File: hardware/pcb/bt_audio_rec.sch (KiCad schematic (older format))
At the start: 61 parts, among them IC1 RN52-I_RM116, IC2 VCNL4200, J1 OutL, J13 Power, J14 PROX Socket, J15 PROX Header, J2 AYF333135, J3 RN52 factory reset, J4 ERM, J5 OutR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

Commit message: Change LED resistor
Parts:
- R13: value 3.6R -> 1.8R
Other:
- note added: "1.8R with 3.3V\nsupply = about\n550mA peak current."
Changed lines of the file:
@@
 P 10100 8500
 F 0 "R13" H 10170 8546 50  0000 L CNN
-F 1 "3.6R" H 10170 8455 50  0000 L CNN
+F 1 "1.8R" H 10170 8455 50  0000 L CNN
 F 2 "Resistor_SMD:R_0603_1608Metric" V 10030 8500 50  0001 C CNN
 F 3 "~" H 10100 8500 50  0001 C CNN
@@
 	0    -1   -1   0
 $EndComp
+Text Notes 10400 8650 0    50   ~ 0
+1.8R with 3.3V\nsupply = about\n550mA peak current.
 $EndSCHEMATC

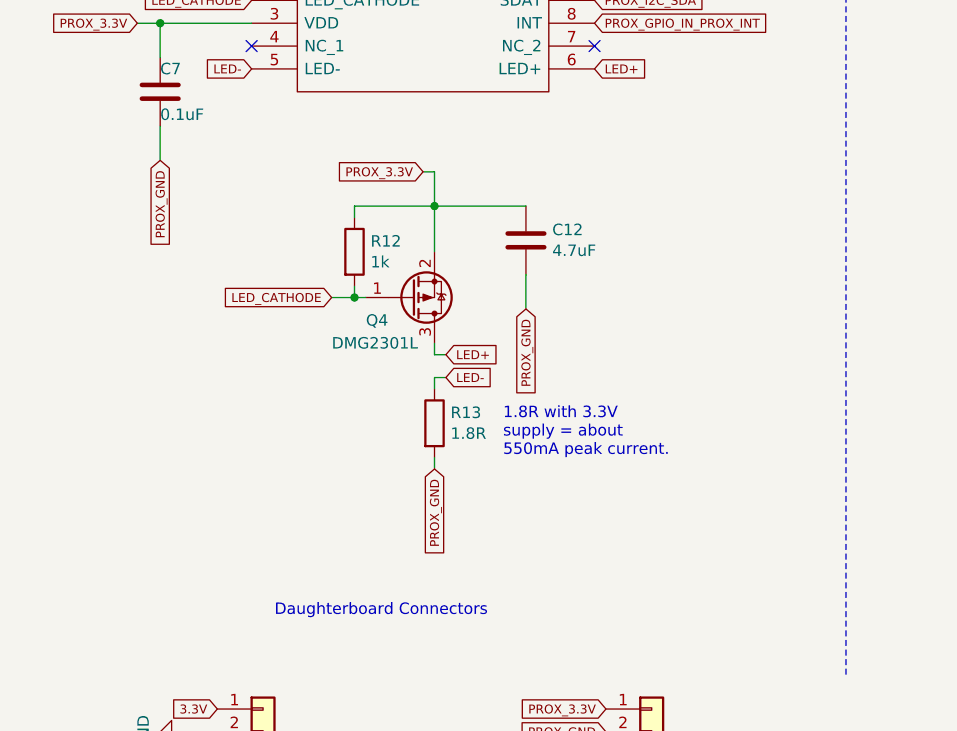
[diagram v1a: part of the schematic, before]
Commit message: Add decoupling cap to proximity LED
See https://www.duk.io/blog/electronics-projects/bt-player/bluetooth-audio-player-firmware
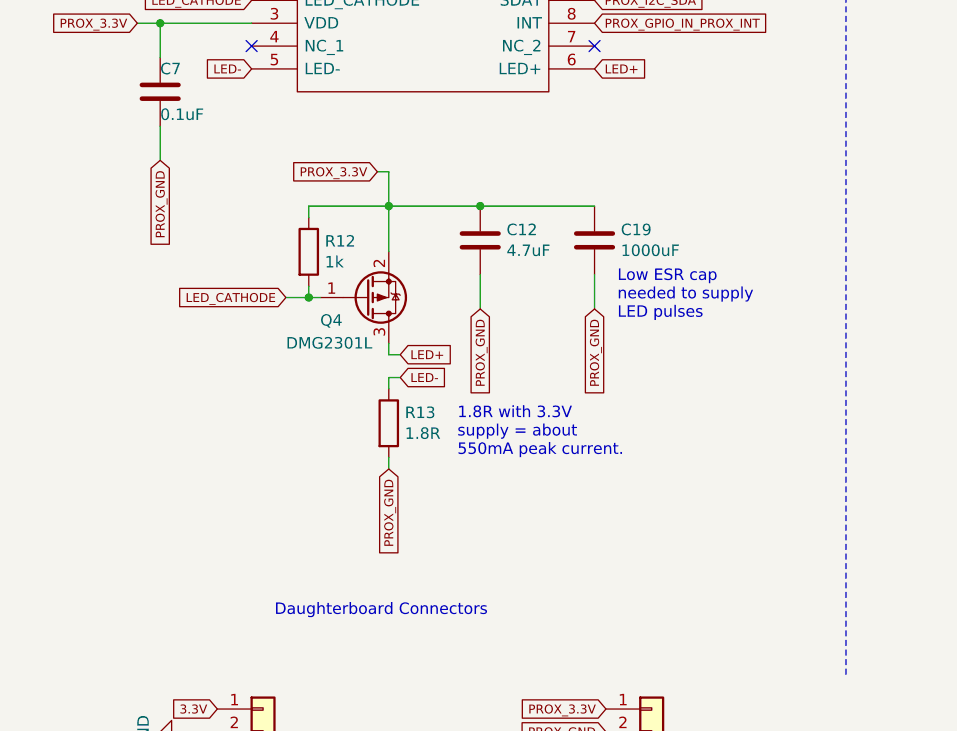
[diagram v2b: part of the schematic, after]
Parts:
- added C19: 1000uF, Capacitor_THT:C_Radial_D6.3mm_H7.0mm_P2.50mm, symbol Device:C
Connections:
- net PROX_3.3V: now also C19.1
- net PROX_GND: now also C19.2
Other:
- note added: "Low ESR cap\nneeded to supply\nLED pulses"
- moved on the sheet: C12, Q4, R12, R13
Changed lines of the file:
@@
 L Transistor_FET:DMG2301L Q4
 U 1 1 5ED5A120
-P 10000 7950
-F 0 "Q4" H 9800 8050 50  0000 L CNN
-F 1 "DMG2301L" H 9650 8150 50  0000 L CNN
-F 2 "Package_TO_SOT_SMD:SOT-23" H 10200 7875 50  0001 L CIN
-F 3 "https://www.diodes.com/assets/Datasheets/DMG2301L.pdf" H 10000 7950 50  0001 L CNN
-	1    10000 7950
+P 9800 7950
+F 0 "Q4" H 9600 8050 50  0000 L CNN
+F 1 "DMG2301L" H 9450 8150 50  0000 L CNN
+F 2 "Package_TO_SOT_SMD:SOT-23" H 10000 7875 50  0001 L CIN
+F 3 "https://www.diodes.com/assets/Datasheets/DMG2301L.pdf" H 9800 7950 50  0001 L CNN
+	1    9800 7950
 	1    0    0    1
 $EndComp
@@
 L Device:R R13
 U 1 1 5ED5AF96
-P 10100 8500
-F 0 "R13" H 10170 8546 50  0000 L CNN
-F 1 "1.8R" H 10170 8455 50  0000 L CNN
-F 2 "Resistor_SMD:R_0603_1608Metric" V 10030 8500 50  0001 C CNN
-F 3 "~" H 10100 8500 50  0001 C CNN
-	1    10100 8500
+P 9900 8500
+F 0 "R13" H 9970 8546 50  0000 L CNN
+F 1 "1.8R" H 9970 8455 50  0000 L CNN
+F 2 "Resistor_SMD:R_0603_1608Metric" V 9830 8500 50  0001 C CNN
+F 3 "~" H 9900 8500 50  0001 C CNN
+	1    9900 8500
 	1    0    0    -1
 $EndComp
@@
 L Device:R R12
 U 1 1 5ED5C408
-P 9750 7750
-F 0 "R12" H 9820 7796 50  0000 L CNN
-F 1 "1k" H 9820 7705 50  0000 L CNN
-F 2 "Resistor_SMD:R_0603_1608Metric" V 9680 7750 50  0001 C CNN
-F 3 "~" H 9750 7750 50  0001 C CNN
-	1    9750 7750
+P 9550 7750
+F 0 "R12" H 9620 7796 50  0000 L CNN
+F 1 "1k" H 9620 7705 50  0000 L CNN
+F 2 "Resistor_SMD:R_0603_1608Metric" V 9480 7750 50  0001 C CNN
+F 3 "~" H 9550 7750 50  0001 C CNN
+	1    9550 7750
 	1    0    0    -1
 $EndComp
@@
 L Device:C C12
 U 1 1 5ED5E36F
-P 10500 7700
-F 0 "C12" H 10615 7746 50  0000 L CNN
-F 1 "4.7uF" H 10615 7655 50  0000 L CNN
-F 2 "Capacitor_SMD:C_0603_1608Metric" H 10538 7550 50  0001 C CNN
-F 3 "~" H 10500 7700 50  0001 C CNN
-	1    10500 7700
-	1    0    0    -1
-$EndComp
-Wire Wire Line
-	9750 7900 9750 7950
-Wire Wire Line
-	9750 7950 9800 7950
-Text GLabel 10050 7400 0    39   Input ~ 0
+P 10300 7700
+F 0 "C12" H 10415 7746 50  0000 L CNN
+F 1 "4.7uF" H 10415 7655 50  0000 L CNN
+F 2 "Capacitor_SMD:C_0603_1608Metric" H 10338 7550 50  0001 C CNN
+F 3 "~" H 10300 7700 50  0001 C CNN
+	1    10300 7700
+	1    0    0    -1
+$EndComp
+Wire Wire Line
+	9550 7900 9550 7950
+Wire Wire Line
+	9550 7950 9600 7950
+Text GLabel 9850 7400 0    39   Input ~ 0
 PROX_3.3V
 Wire Wire Line
-	9750 7600 9750 7550
-Wire Wire Line
-	9750 7550 10100 7550
-Connection ~ 10100 7550
-Wire Wire Line
-	10100 7550 10100 7750
+	9550 7600 9550 7550
+Wire Wire Line
+	9550 7550 9900 7550
+Connection ~ 9900 7550
+Wire Wire Line
+	9900 7550 9900 7750
 Text GLabel 10800 6950 2    39   Input ~ 0
 LED+
-Text GLabel 10150 8200 2    39   Input ~ 0
+Text GLabel 9950 8200 2    39   Input ~ 0
 LED+
 Wire Wire Line
-	10100 8200 10150 8200
+	9900 8200 9950 8200
 Text GLabel 9300 6650 0    39   Input ~ 0
 LED_CATHODE
-Text GLabel 9650 7950 0    39   Input ~ 0
+Text GLabel 9450 7950 0    39   Input ~ 0
 LED_CATHODE
 Text GLabel 8800 6750 0    39   Input ~ 0
 PROX_3.3V
-Text GLabel 10150 8300 2    39   Input ~ 0
+Text GLabel 9950 8300 2    39   Input ~ 0
 LED-
 Wire Wire Line
-	10150 8300 10100 8300
+	9950 8300 9900 8300
 Text GLabel 9300 6950 0    39   Input ~ 0
 LED-
 Wire Wire Line
-	10100 8300 10100 8350
-Wire Wire Line
-	10100 8150 10100 8200
-Wire Wire Line
-	10100 7400 10100 7550
-Wire Wire Line
-	10050 7400 10100 7400
-Wire Wire Line
-	10500 7550 10100 7550
+	9900 8300 9900 8350
+Wire Wire Line
+	9900 8150 9900 8200
+Wire Wire Line
+	9900 7400 9900 7550
+Wire Wire Line
+	9850 7400 9900 7400
+Wire Wire Line
+	10300 7550 9900 7550
 $Comp
 L BOB_General:MCP1661 U2
@@
 Wire Wire Line
 	8900 7200 8900 7350
-Text GLabel 10100 8700 3    39   Input ~ 0
+Text GLabel 9900 8700 3    39   Input ~ 0
 PROX_GND
 Text GLabel 10850 10050 0    39   Input ~ 0
@@
 	1    0    0    -1
 $EndComp
-Text GLabel 10500 8000 3    39   Input ~ 0
+Text GLabel 10300 8000 3    39   Input ~ 0
 PROX_GND
 Wire Wire Line
-	10500 7850 10500 8000
+	10300 7850 10300 8000
 Text GLabel 8850 6550 0    39   Input ~ 0
 PROX_GND
@@
 PROX_GND
 Wire Wire Line
-	9650 7950 9750 7950
-Connection ~ 9750 7950
+	9450 7950 9550 7950
+Connection ~ 9550 7950
 $Comp
 L Connector:Conn_01x02_Male J4
@@
 	9500 3750 10050 3750
 Wire Wire Line
-	10100 8650 10100 8700
+	9900 8650 9900 8700
 Wire Notes Line
 	8150 10850 8150 3250
@@
 $EndComp
 $Comp
-L power:GND #PWR?
+L power:GND #PWR0127
 U 1 1 5F6D837E
 P 6900 2350
-F 0 "#PWR?" H 6900 2100 50  0001 C CNN
+F 0 "#PWR0127" H 6900 2100 50  0001 C CNN
 F 1 "GND" V 6900 2150 50  0000 C CNN
 F 2 "" H 6900 2350 50  0001 C CNN
@@
 $EndComp
 $Comp
-L power:GND #PWR?
+L power:GND #PWR0135
 U 1 1 5F6D7473
 P 5600 2150
-F 0 "#PWR?" H 5600 1900 50  0001 C CNN
+F 0 "#PWR0135" H 5600 1900 50  0001 C CNN
 F 1 "GND" V 5600 1950 50  0000 C CNN
 F 2 "" H 5600 2150 50  0001 C CNN
@@
 $EndComp
 $Comp
-L power:GND #PWR?
+L power:GND #PWR0136
 U 1 1 5F6D5888
 P 5600 2050
-F 0 "#PWR?" H 5600 1800 50  0001 C CNN
+F 0 "#PWR0136" H 5600 1800 50  0001 C CNN
 F 1 "GND" V 5600 1850 50  0000 C CNN
 F 2 "" H 5600 2050 50  0001 C CNN
@@
 $EndComp
 $Comp
-L power:GND #PWR?
+L power:GND #PWR0137
 U 1 1 5F6D3DCB
 P 5600 2850
-F 0 "#PWR?" H 5600 2600 50  0001 C CNN
+F 0 "#PWR0137" H 5600 2600 50  0001 C CNN
 F 1 "GND" V 5600 2650 50  0000 C CNN
 F 2 "" H 5600 2850 50  0001 C CNN
@@
 $EndComp
 $Comp
-L power:GND #PWR?
+L power:GND #PWR0138
 U 1 1 5F6DA8CC
 P 6900 2750
-F 0 "#PWR?" H 6900 2500 50  0001 C CNN
+F 0 "#PWR0138" H 6900 2500 50  0001 C CNN
 F 1 "GND" V 6900 2550 50  0000 C CNN
 F 2 "" H 6900 2750 50  0001 C CNN
@@
 $EndComp
 $Comp
-L power:GND #PWR?
+L power:GND #PWR0139
 U 1 1 5F6DAF32
 P 6900 3150
-F 0 "#PWR?" H 6900 2900 50  0001 C CNN
+F 0 "#PWR0139" H 6900 2900 50  0001 C CNN
 F 1 "GND" V 6900 2950 50  0000 C CNN
 F 2 "" H 6900 3150 50  0001 C CNN
@@
 $EndComp
 $Comp
-L power:GND #PWR?
+L power:GND #PWR0140
 U 1 1 5F6E1B6C
 P 6900 3850
-F 0 "#PWR?" H 6900 3600 50  0001 C CNN
+F 0 "#PWR0140" H 6900 3600 50  0001 C CNN
 F 1 "GND" V 6900 3650 50  0000 C CNN
 F 2 "" H 6900 3850 50  0001 C CNN
@@
 	0    -1   -1   0
 $EndComp
-Text Notes 10400 8650 0    50   ~ 0
+Text Notes 10200 8650 0    50   ~ 0
 1.8R with 3.3V\nsupply = about\n550mA peak current.
+$Comp
+L Device:C C19
+U 1 1 5F87451F
+P 10800 7700
+F 0 "C19" H 10915 7746 50  0000 L CNN
+F 1 "1000uF" H 10915 7655 50  0000 L CNN
+F 2 "Capacitor_THT:C_Radial_D6.3mm_H7.0mm_P2.50mm" H 10838 7550 50  0001 C CNN
+F 3 "~" H 10800 7700 50  0001 C CNN
+	1    10800 7700
+	1    0    0    -1
+$EndComp
+Text GLabel 10800 8000 3    39   Input ~ 0
+PROX_GND
+Wire Wire Line
+	10800 7850 10800 8000
+Wire Wire Line
+	10300 7550 10800 7550
+Connection ~ 10300 7550
+Text Notes 10900 8050 0    50   ~ 0
+Low ESR cap\nneeded to supply\nLED pulses
 $EndSCHEMATC

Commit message: Add flyback label
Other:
- note added: "Haptic Feedback\n(motor requires flyback diode)"
- note removed: "Haptic Feedback"
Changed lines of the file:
@@
 Text Notes 12850 5450 0    50   ~ 0
 (Viref - Vss) / Iref\nIref = 15.625μA\n= 515k@8.04V
-Text Notes 3600 9400 0    50   ~ 0
-Haptic Feedback
+Text Notes 3300 9450 0    50   ~ 0
+Haptic Feedback\n(motor requires flyback diode)
 Connection ~ 13050 3350
 Text GLabel 5600 2550 0    39   Input ~ 0
